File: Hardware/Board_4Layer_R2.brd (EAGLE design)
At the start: 108 x 45.7 mm, 57 parts, among them U1 EDISON_CONNECTOR_FULLMOUNTING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, U2 LAN9512-JZX, U3 MAX4995AAUT+, U4 EDISON_CONNECTOR_FULLHEADER, X1 J1011F01P

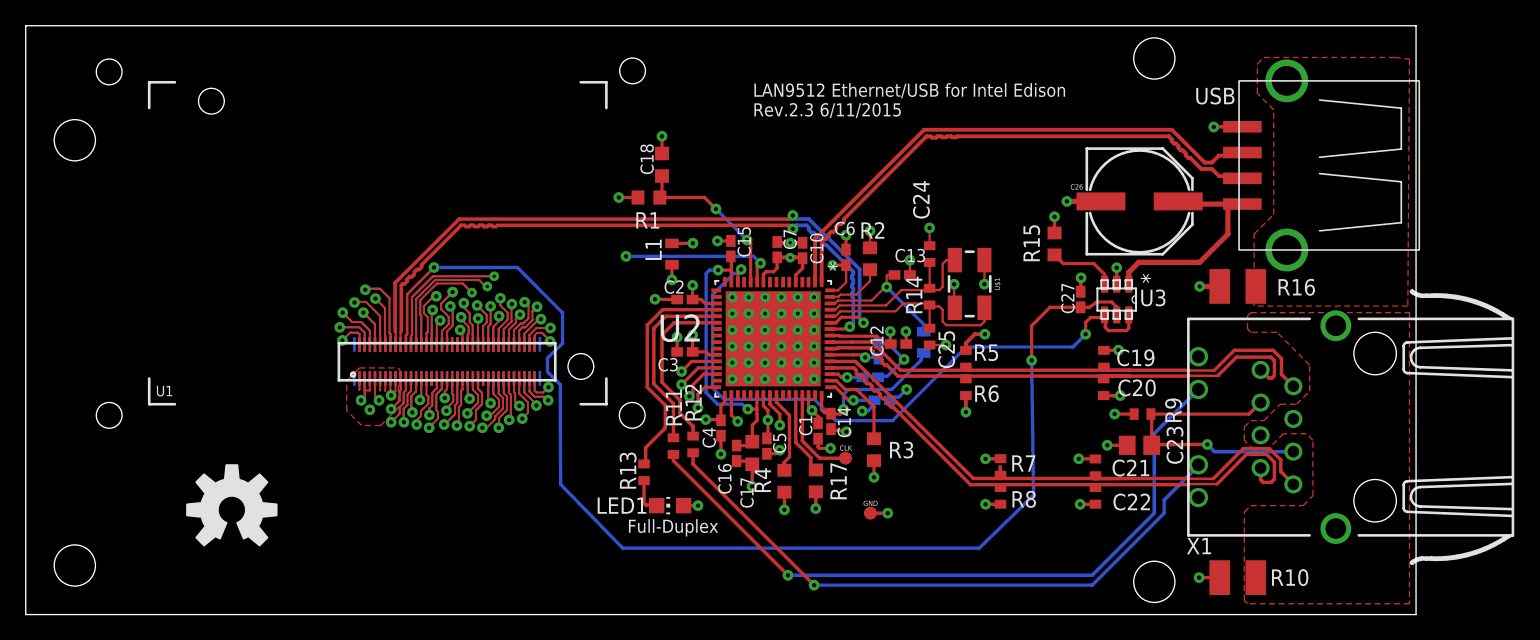
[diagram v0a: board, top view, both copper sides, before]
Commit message: Fixed board inconsistencies, airwires, stubs, etc. Passes FreeDFM.com checks with no errors and warnings. Exported CAM files.
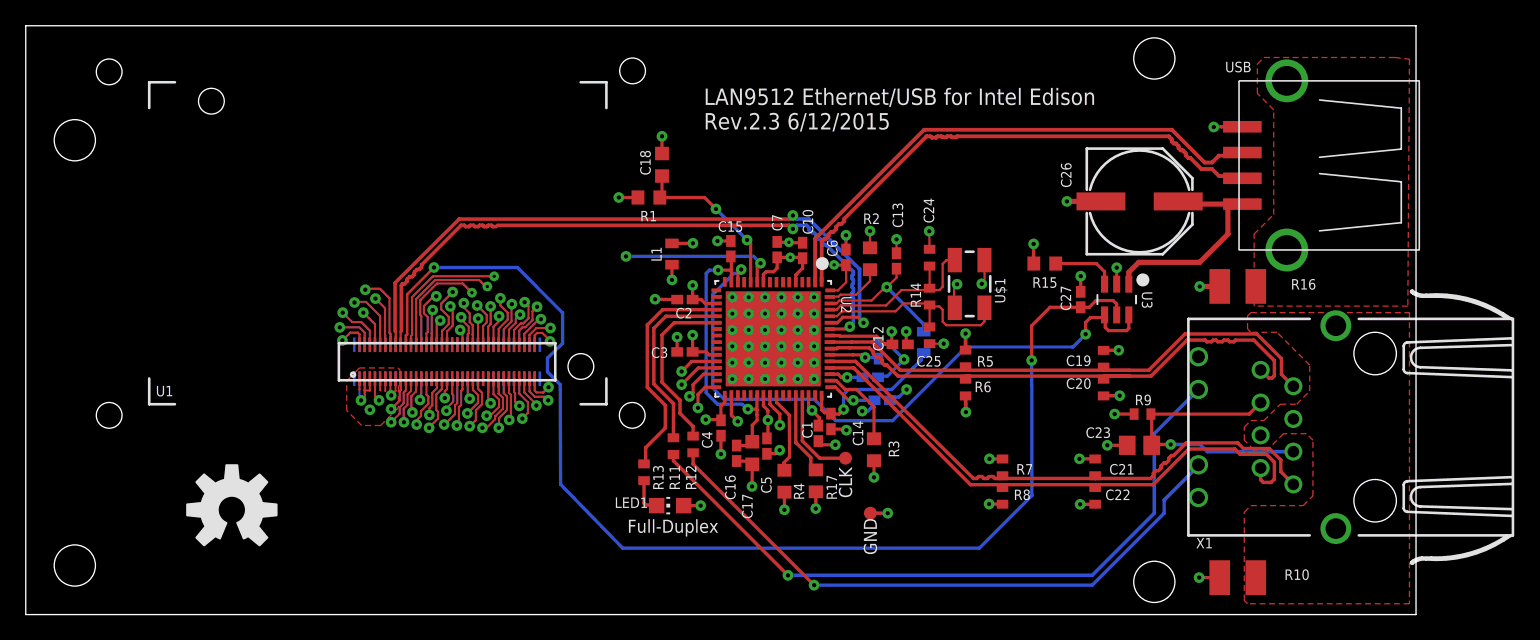
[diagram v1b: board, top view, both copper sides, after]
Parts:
- moved R15 1.70 mm to (77.9, 27.3), turned to 0 degrees
- moved C13 1.17 mm to (66.3, 27.5), turned to 90 degrees
- moved C24 0.28 mm to (68.9, 27.7)
- moved C1 0.18 mm to (60.3, 14.1)
- moved R7 0.16 mm to (74.6, 11.4)
- moved R8 0.15 mm to (74.6, 9.22)
- moved C12 0.13 mm to (66.6, 21.0)
- moved C25 0.10 mm to (68.9, 21.7)
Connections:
- new net S$10: U4.61
- new net S$3: U4.16
- new net S$9: U1.53
- net P37: no longer U1.37
- net P41: no longer U1.41
- net P43: no longer U1.43
- net P47: no longer U4.47
- net P53: no longer U1.53
- net P61: no longer U4.61
- net USBUP_N: no longer U4.18
- net USBUP_P: no longer U4.16
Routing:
- net S$9: track 0.00 -> 7.10 mm, vias 0 -> 1
- net P53: track 6.97 -> 0.51 mm, vias 1 -> 0
- net RX_P: track 47.1 -> 43.9 mm
- net GND: track 66.1 -> 69.1 mm
- net P55: track 9.36 -> 10.9 mm
- net TX_P: track 41.7 -> 43.1 mm
- net P51: track 3.70 -> 4.87 mm
- net VDD33A: track 38.1 -> 37.0 mm
- net TX_N: track 42.1 -> 43.1 mm
- net P7: track 3.36 -> 4.15 mm
- net P33: track 8.06 -> 8.80 mm
- net P31: track 5.69 -> 6.36 mm
- net P61: track 0.00 -> 0.66 mm
- net P21: track 7.00 -> 7.64 mm
- net P39: track 7.56 -> 8.18 mm
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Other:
- board text added: "LAN9512 Ethernet/USB for Intel Edison Rev.2.3 6/12/2015"
- board text removed: "LAN9512 Ethernet/USB for Intel Edison Rev.2.3 6/11/2015"
